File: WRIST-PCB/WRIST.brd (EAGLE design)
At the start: 56.3 x 16.5 mm, 44 parts, among them Q3 BSS138, U3 LP5907-2.8V

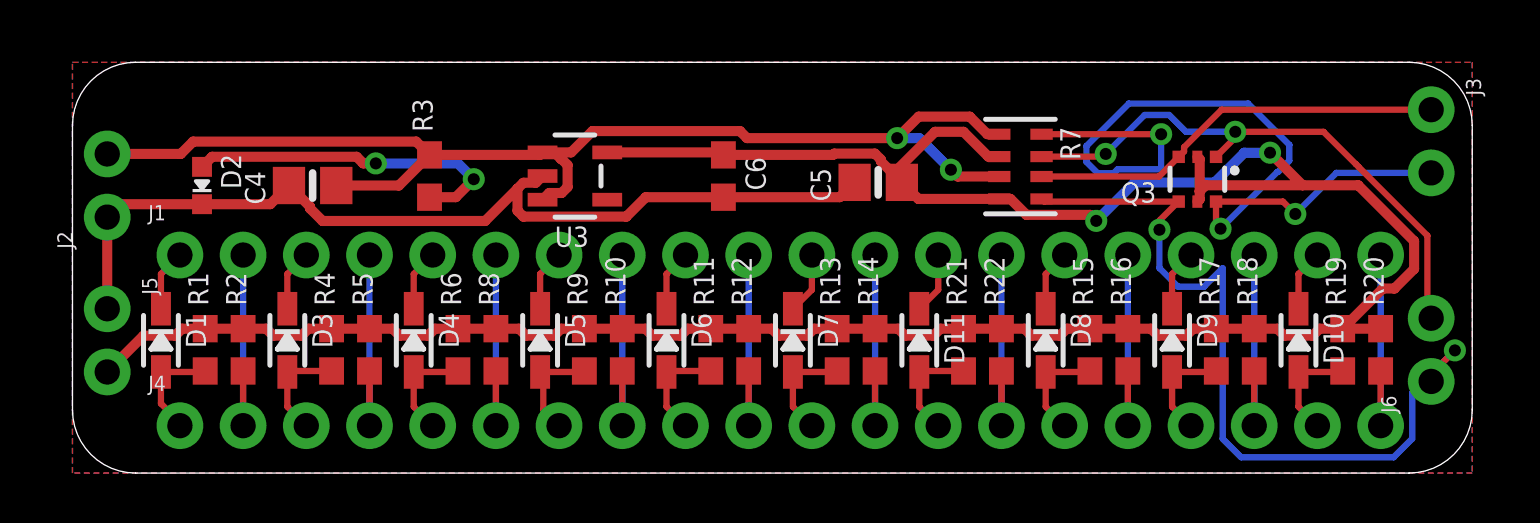
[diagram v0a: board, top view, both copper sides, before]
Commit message: update pcb through holes and design
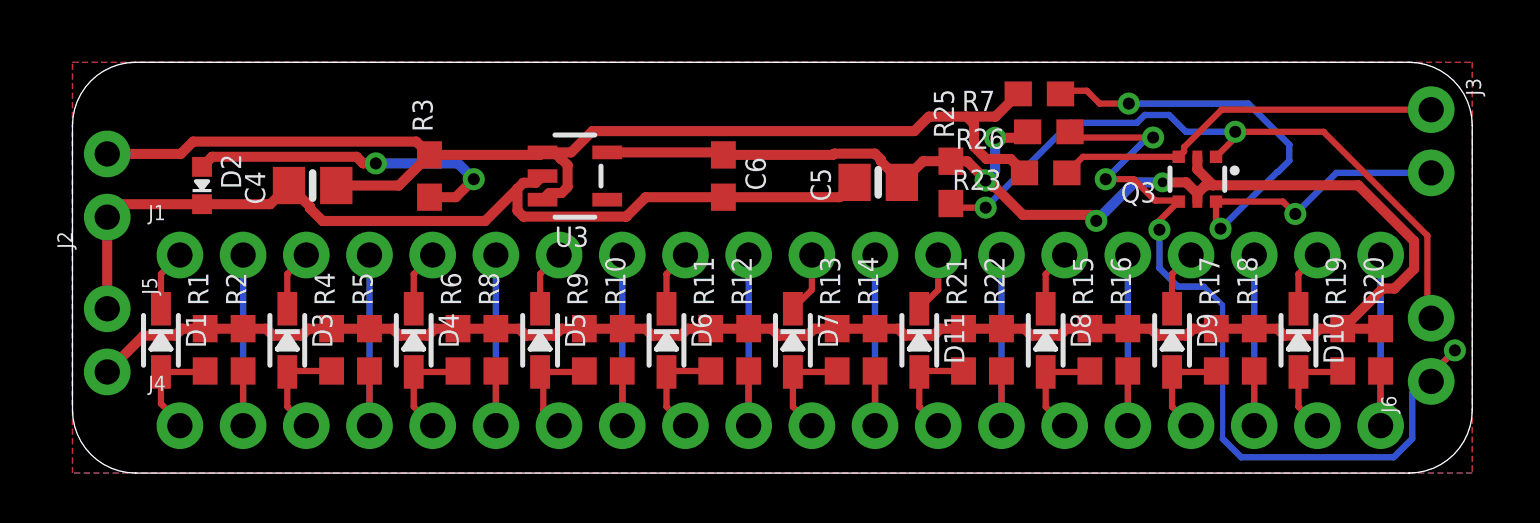
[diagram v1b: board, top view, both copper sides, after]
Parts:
- added R23, R25, R26: 10K, microbuilder:0603-NO
- R7: device microbuilder:RESPACK_4X0603 -> microbuilder:0603-NO
- moved R7 3.02 mm to (38.9, 15.2), turned to 180 degrees
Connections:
- net 2.8V: now also R25.2, R26.2; no longer R7.2, R7.4
- net SCL: now also R7.1; no longer R7.8
- net SCL_3V: now also R25.1; no longer R7.7
- net SDA: now also R23.1; no longer R7.6
- net SDA_3V: now also R26.1; no longer R7.5
- net VCC: now also R23.2, R7.2; no longer R7.1, R7.3
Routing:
- net SCL: track 34.9 -> 25.4 mm
- net 2.8V: track 106.7 -> 100.7 mm, vias 2 -> 4
- net SCL_3V: track 22.9 -> 27.5 mm
- net SDA_3V: track 32.7 -> 35.0 mm, vias 2 -> 4
- net SDA: track 16.9 -> 15.8 mm
- net VCC: track 49.8 -> 49.5 mm, vias 2 -> 0

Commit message: add text to wrist
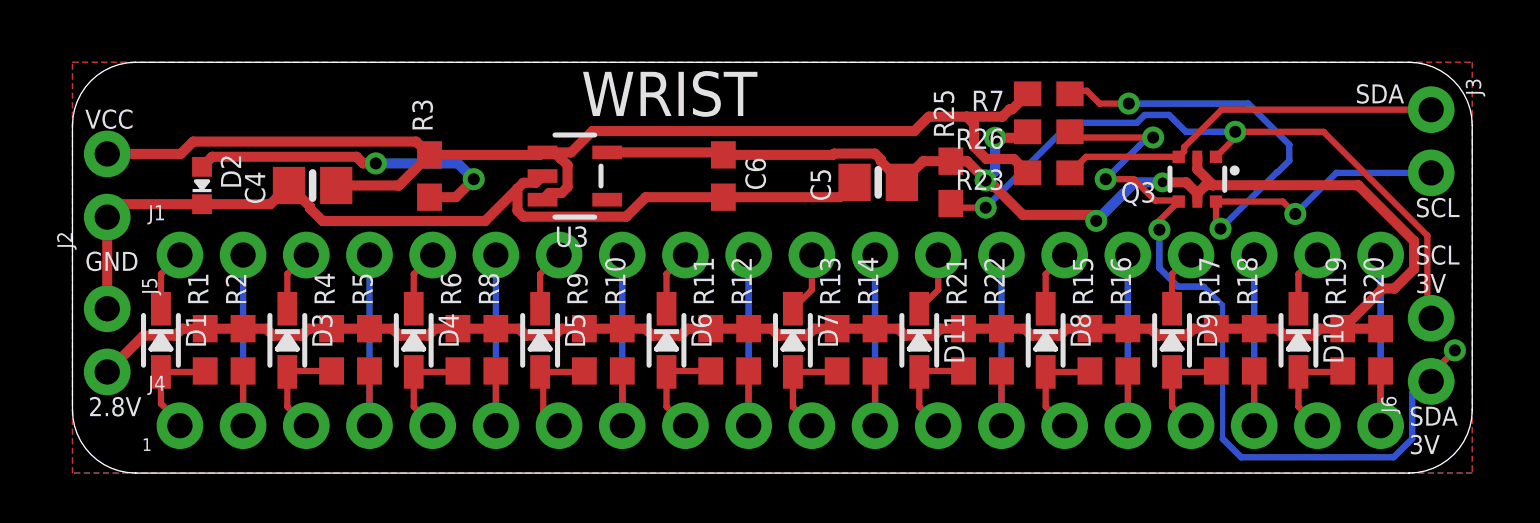
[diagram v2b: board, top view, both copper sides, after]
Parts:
- moved R7 0.38 mm to (39.2, 15.2)
- moved R23 0.13 mm to (39.2, 12.1)
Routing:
- net VCC: track 49.5 -> 50.0 mm
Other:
- board text added: "1"
- board text added: "2.8V"
- board text added: "GND"
- board text added: "SCL"
- board text added: "SCL 3V"
- board text added: "SDA"
- board text added: "SDA 3V"
- board text added: "VCC"
- board text added: "WRIST"
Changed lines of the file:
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@@
 <dimension x1="25.4" y1="9.144" x2="0" y2="6.223" x3="12.7" y3="-6.223" textsize="1.778" layer="47" dtype="horizontal" unit="inch"/>
 <dimension x1="13.208" y1="0" x2="12.319" y2="17.78" x3="32.131" y3="8.89" textsize="1.778" layer="47" dtype="vertical" unit="inch"/>
+<text x="0.508" y="13.843" size="0.762" layer="21">VCC</text>
+<text x="0.508" y="8.128" size="0.762" layer="21">GND</text>
+<text x="51.562" y="14.859" size="0.762" layer="21">SDA</text>
+<text x="53.975" y="10.287" size="0.762" layer="21">SCL</text>
+<text x="53.975" y="7.239" size="0.762" layer="21">SCL
+3V</text>
+<text x="53.721" y="0.762" size="0.762" layer="21">SDA
+3V</text>
+<text x="0.635" y="2.286" size="0.762" layer="21">2.8V</text>
+<text x="2.794" y="0.889" size="0.508" layer="21">1</text>
+<text x="20.447" y="14.351" size="1.778" layer="21">WRIST</text>
 </plain>
 <attributes>
@@
 <attribute name="VALUE" x="38.1" y="6.731" size="0.4064" layer="27" font="vector" ratio="10" rot="R90"/>
 </element>
-<element name="R7" library="microbuilder" package="0603-NO" value="10K" x="38.862" y="15.24" smashed="yes" rot="R180">
-<attribute name="NAME" x="37.084" y="15.367" size="0.8128" layer="25" font="vector" ratio="18" rot="R180"/>
-<attribute name="VALUE" x="37.084" y="16.002" size="0.4064" layer="27" font="vector" ratio="10" rot="R180"/>
-</element>
-<element name="R23" library="microbuilder" package="0603-NO" value="10K" x="39.116" y="12.065" smashed="yes" rot="R180">
-<attribute name="NAME" x="37.338" y="12.192" size="0.8128" layer="25" font="vector" ratio="18" rot="R180"/>
-<attribute name="VALUE" x="37.338" y="12.827" size="0.4064" layer="27" font="vector" ratio="10" rot="R180"/>
+<element name="R7" library="microbuilder" package="0603-NO" value="10K" x="39.243" y="15.24" smashed="yes" rot="R180">
+<attribute name="NAME" x="37.465" y="15.367" size="0.8128" layer="25" font="vector" ratio="18" rot="R180"/>
+<attribute name="VALUE" x="37.465" y="16.002" size="0.4064" layer="27" font="vector" ratio="10" rot="R180"/>
+</element>
+<element name="R23" library="microbuilder" package="0603-NO" value="10K" x="39.243" y="12.065" smashed="yes" rot="R180">
+<attribute name="NAME" x="37.465" y="12.192" size="0.8128" layer="25" font="vector" ratio="18" rot="R180"/>
+<attribute name="VALUE" x="37.465" y="12.827" size="0.4064" layer="27" font="vector" ratio="10" rot="R180"/>
 </element>
 <element name="R25" library="microbuilder" package="0603-NO" value="10K" x="35.306" y="11.684" smashed="yes" rot="R90">
@@
 <wire x1="46.189025" y1="14.605" x2="54.61" y2="14.605" width="0.254" layer="1"/>
 <contactref element="R23" pad="1"/>
-<wire x1="39.966" y1="12.065" x2="40.612" y2="12.711" width="0.254" layer="1"/>
-<wire x1="40.612" y1="12.711" x2="44.462" y2="12.711" width="0.254" layer="1"/>
+<wire x1="40.093" y1="12.065" x2="40.739" y2="12.711" width="0.254" layer="1"/>
+<wire x1="40.739" y1="12.711" x2="44.462" y2="12.711" width="0.254" layer="1"/>
 </signal>
 <signal name="SCL">
@@
 <wire x1="42.45730625" y1="14.8509" x2="41.2831" y2="14.8509" width="0.254" layer="1"/>
 <wire x1="41.2831" y1="14.8509" x2="40.767" y2="15.367" width="0.254" layer="1"/>
-<wire x1="40.767" y1="15.367" x2="39.839" y2="15.367" width="0.254" layer="1"/>
-<wire x1="39.839" y1="15.367" x2="39.712" y2="15.24" width="0.254" layer="1"/>
+<wire x1="40.767" y1="15.367" x2="40.22" y2="15.367" width="0.254" layer="1"/>
+<wire x1="40.22" y1="15.367" x2="40.093" y2="15.24" width="0.254" layer="1"/>
 </signal>
 <signal name="GND">
@@
 <contactref element="R23" pad="2"/>
 <wire x1="33.83729375" y1="13.7444" x2="34.41849375" y2="14.3256" width="0.4064" layer="1"/>
-<wire x1="37.0976" y1="14.3256" x2="38.012" y2="15.24" width="0.4064" layer="1"/>
 <wire x1="34.41849375" y1="14.3256" x2="35.941" y2="14.3256" width="0.4064" layer="1"/>
-<wire x1="35.941" y1="14.3256" x2="37.0976" y2="14.3256" width="0.4064" layer="1"/>
 <wire x1="20.8997625" y1="13.7444" x2="33.83729375" y2="13.7444" width="0.4064" layer="1"/>
 <wire x1="36.73154375" y1="12.6238" x2="36.2331" y2="13.12224375" width="0.4064" layer="1"/>
-<wire x1="38.266" y1="12.065" x2="37.7072" y2="12.6238" width="0.4064" layer="1"/>
-<wire x1="37.7072" y1="12.6238" x2="36.73154375" y2="12.6238" width="0.4064" layer="1"/>
+<wire x1="38.393" y1="12.065" x2="37.8342" y2="12.6238" width="0.4064" layer="1"/>
+<wire x1="37.8342" y1="12.6238" x2="36.73154375" y2="12.6238" width="0.4064" layer="1"/>
 <wire x1="36.2331" y1="13.12224375" x2="36.2331" y2="14.0335" width="0.4064" layer="1"/>
 <wire x1="36.2331" y1="14.0335" x2="35.941" y2="14.3256" width="0.4064" layer="1"/>
+<wire x1="38.393" y1="15.24" x2="37.7754" y2="14.6224" width="0.4064" layer="1"/>
+<wire x1="37.7754" y1="14.6224" x2="37.6746625" y2="14.6224" width="0.4064" layer="1"/>
+<wire x1="37.3778625" y1="14.3256" x2="35.941" y2="14.3256" width="0.4064" layer="1"/>
+<wire x1="37.6746625" y1="14.6224" x2="37.3778625" y2="14.3256" width="0.4064" layer="1"/>
 </signal>
 <signal name="N$1">
@@
 </drawing>
 <compatibility>
+<note version="6.3" minversion="6.2.2" severity="warning">
+Since Version 6.2.2 text objects can contain more than one line,
+which will not be processed correctly with this version.
+</note>
 <note version="8.2" severity="warning">
 Since Version 8.2, EAGLE supports online libraries. The ids

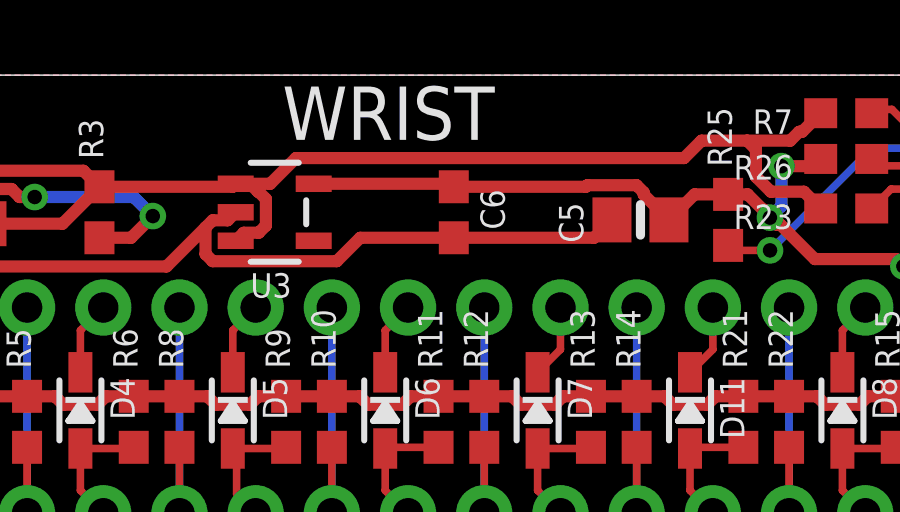
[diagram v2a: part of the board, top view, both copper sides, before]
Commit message: replace smt capacitor with holes
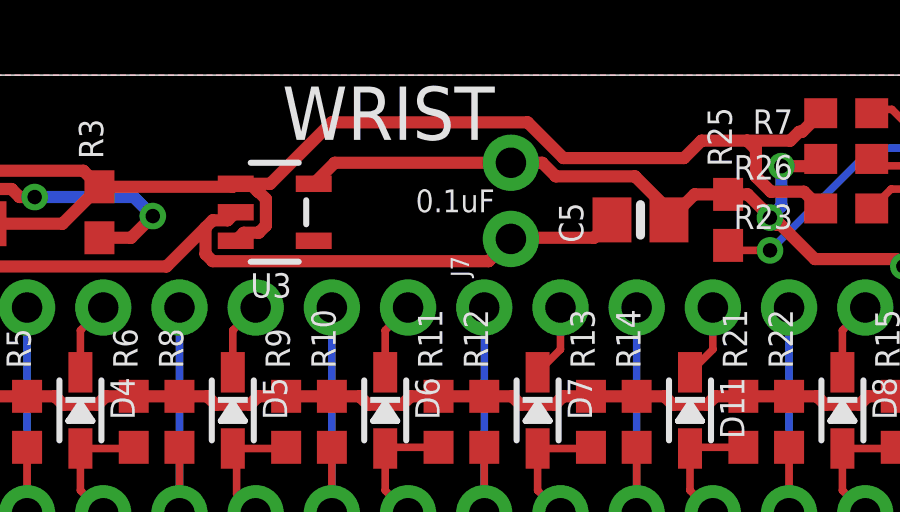
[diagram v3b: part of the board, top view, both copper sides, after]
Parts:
- removed C6: 0.1uF, microbuilder:0603-NO
- added J7: (no value), SparkFun-Connectors:1X02_NO_SILK
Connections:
- net 2.8V: now also J7.2; no longer C6.1
- net GND: now also J7.1; no longer C6.2
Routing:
- net VCC: track 50.0 -> 51.0 mm
- net 2.8V: track 100.7 -> 101.3 mm
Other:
- board text added: "0.1uF"
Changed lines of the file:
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@@
 <text x="2.794" y="0.889" size="0.508" layer="21">1</text>
 <text x="20.447" y="14.351" size="1.778" layer="21">WRIST</text>
+<text x="24.892" y="11.938" size="0.762" layer="21">0.1uF</text>
 </plain>
 <attributes>
@@
 <attribute name="VALUE" x="30.861" y="9.271" size="1.016" layer="27" ratio="10"/>
 </element>
-<element name="C6" library="microbuilder" package="0603-NO" value="0.1uF" x="26.162" y="11.938" smashed="yes" rot="R270">
-<attribute name="NAME" x="27.051" y="12.7" size="0.8128" layer="25" ratio="18" rot="R270"/>
-<attribute name="VALUE" x="26.67" y="13.335" size="1.016" layer="27" ratio="10" rot="R90"/>
-</element>
 <element name="Q3" library="microbuilder" package="SOT363" value="BSS138" x="45.212" y="11.811" smashed="yes" rot="R180">
 <attribute name="NAME" x="43.561" y="11.684" size="0.8128" layer="25" ratio="18" rot="R180"/>
@@
 <attribute name="NAME" x="37.465" y="13.843" size="0.8128" layer="25" font="vector" ratio="18" rot="R180"/>
 <attribute name="VALUE" x="37.465" y="14.478" size="0.4064" layer="27" font="vector" ratio="10" rot="R180"/>
+</element>
+<element name="J7" library="SparkFun-Connectors" library_urn="urn:adsk.eagle:library:513" package="1X02_NO_SILK" package3d_urn="urn:adsk.eagle:package:38051/1" value="" x="28.067" y="11.049" smashed="yes" rot="R90">
+<attribute name="NAME" x="26.67" y="9.779" size="0.6096" layer="25" font="vector" ratio="20" rot="R90"/>
+<attribute name="VALUE" x="30.099" y="9.779" size="0.6096" layer="27" font="vector" ratio="20" rot="R90"/>
 </element>
 </elements>
@@
 <contactref element="U3" pad="2"/>
 <contactref element="C5" pad="2"/>
-<contactref element="C6" pad="2"/>
 <polygon width="0.254" layer="1">
 <vertex x="0" y="16.51"/>
@@
 <wire x1="5.207" y1="10.807" x2="7.952" y2="10.807" width="0.4064" layer="1"/>
 <wire x1="7.952" y1="10.807" x2="8.702" y2="11.557" width="0.4064" layer="1"/>
-<wire x1="26.162" y1="11.088" x2="30.839" y2="11.088" width="0.4064" layer="1"/>
 <wire x1="30.839" y1="11.088" x2="31.435" y2="11.684" width="0.4064" layer="1"/>
-<wire x1="18.1245625" y1="10.3066" x2="17.8865" y2="10.5446625" width="0.4064" layer="1"/>
+<wire x1="17.8865" y1="10.5446625" x2="18.1245625" y2="10.3066" width="0.4064" layer="1"/>
 <wire x1="17.8865" y1="10.5446625" x2="17.8865" y2="11.4313375" width="0.4064" layer="1"/>
 <wire x1="17.8865" y1="11.4313375" x2="18.1245625" y2="11.6694" width="0.4064" layer="1"/>
-<wire x1="26.162" y1="11.088" x2="23.0428375" y2="11.088" width="0.4064" layer="1"/>
-<wire x1="23.0428375" y1="11.088" x2="22.2614375" y2="10.3066" width="0.4064" layer="1"/>
-<wire x1="22.2614375" y1="10.3066" x2="18.1245625" y2="10.3066" width="0.4064" layer="1"/>
 <wire x1="18.1245625" y1="11.6694" x2="18.6243" y2="11.6694" width="0.4064" layer="1"/>
 <wire x1="18.6243" y1="11.6694" x2="18.8929" y2="11.938" width="0.4064" layer="1"/>
@@
 <wire x1="10.0526625" y1="10.1316" x2="16.5867625" y2="10.1316" width="0.4064" layer="1"/>
 <wire x1="16.5867625" y1="10.1316" x2="17.8865" y2="11.4313375" width="0.4064" layer="1"/>
+<contactref element="J7" pad="1"/>
+<wire x1="27.3246" y1="10.3066" x2="28.067" y2="11.049" width="0.4064" layer="1"/>
+<wire x1="18.1245625" y1="10.3066" x2="27.3246" y2="10.3066" width="0.4064" layer="1"/>
+<wire x1="28.067" y1="11.049" x2="28.106" y2="11.088" width="0.4064" layer="1"/>
+<wire x1="28.106" y1="11.088" x2="30.839" y2="11.088" width="0.4064" layer="1"/>
 </signal>
 <signal name="XSHUT_1">
@@
 </signal>
 <signal name="2.8V">
-<contactref element="C6" pad="1"/>
 <contactref element="U3" pad="5"/>
 <contactref element="C5" pad="1"/>
@@
 <wire x1="2.8556" y1="5.5226" x2="4.1243375" y2="5.5226" width="0.4064" layer="1"/>
 <wire x1="4.1243375" y1="5.5226" x2="4.4047375" y2="5.803" width="0.4064" layer="1"/>
-<wire x1="21.4931" y1="12.888" x2="26.062" y2="12.888" width="0.4064" layer="1"/>
-<wire x1="26.062" y1="12.888" x2="26.162" y2="12.788" width="0.4064" layer="1"/>
-<wire x1="26.162" y1="12.788" x2="30.5642625" y2="12.788" width="0.4064" layer="1"/>
-<wire x1="30.5642625" y1="12.788" x2="30.6166625" y2="12.8404" width="0.4064" layer="1"/>
-<wire x1="30.6166625" y1="12.8404" x2="32.2533375" y2="12.8404" width="0.4064" layer="1"/>
-<wire x1="32.2533375" y1="12.8404" x2="32.4914" y2="12.6023375" width="0.4064" layer="1"/>
-<wire x1="32.4914" y1="12.6023375" x2="32.4914" y2="12.5276" width="0.4064" layer="1"/>
-<wire x1="32.4914" y1="12.5276" x2="33.335" y2="11.684" width="0.4064" layer="1"/>
 <wire x1="53.13561875" y1="7.4168" x2="53.9242" y2="8.20538125" width="0.4064" layer="1"/>
 <wire x1="53.9242" y1="8.20538125" x2="53.9242" y2="9.32061875" width="0.4064" layer="1"/>
@@
 <wire x1="44.7637375" y1="11.684" x2="45.212" y2="11.2357375" width="0.4064" layer="1"/>
 <wire x1="41.148" y1="10.1363" x2="42.6957" y2="11.684" width="0.4064" layer="16"/>
-<wire x1="33.335" y1="11.684" x2="34.185" y2="12.534" width="0.4064" layer="1"/>
+<wire x1="33.335" y1="11.684" x2="33.495" y2="11.844" width="0.4064" layer="1"/>
+<wire x1="33.495" y1="11.844" x2="34.185" y2="12.534" width="0.4064" layer="1"/>
 <wire x1="34.185" y1="12.534" x2="35.306" y2="12.534" width="0.4064" layer="1"/>
 <via x="36.69960625" y="11.7602" extent="1-16" drill="0.4826"/>
@@
 <wire x1="36.4790375" y1="12.0142" x2="36.56015625" y2="12.0142" width="0.4064" layer="1"/>
 <wire x1="36.56015625" y1="12.0142" x2="37.05545625" y2="11.5189" width="0.4064" layer="1"/>
+<contactref element="J7" pad="2"/>
+<wire x1="21.4931" y1="12.888" x2="22.1941" y2="13.589" width="0.4064" layer="1"/>
+<wire x1="22.1941" y1="13.589" x2="28.067" y2="13.589" width="0.4064" layer="1"/>
+<wire x1="28.067" y1="13.589" x2="29.1087125" y2="13.589" width="0.4064" layer="1"/>
+<wire x1="29.1087125" y1="13.589" x2="29.5629125" y2="13.1348" width="0.4064" layer="1"/>
+<wire x1="32.2042" y1="13.1348" x2="33.495" y2="11.844" width="0.4064" layer="1"/>
+<wire x1="29.5629125" y1="13.1348" x2="32.2042" y2="13.1348" width="0.4064" layer="1"/>
 </signal>
 <signal name="SCL_3V">
@@
 <wire x1="13.816" y1="13.323" x2="14.351" y2="12.788" width="0.4064" layer="1"/>
 <wire x1="18.8929" y1="12.888" x2="20.0433625" y2="12.888" width="0.4064" layer="1"/>
-<wire x1="20.0433625" y1="12.888" x2="20.8997625" y2="13.7444" width="0.4064" layer="1"/>
 <contactref element="R7" pad="2"/>
 <contactref element="R23" pad="2"/>
 <wire x1="33.83729375" y1="13.7444" x2="34.41849375" y2="14.3256" width="0.4064" layer="1"/>
 <wire x1="34.41849375" y1="14.3256" x2="35.941" y2="14.3256" width="0.4064" layer="1"/>
-<wire x1="20.8997625" y1="13.7444" x2="33.83729375" y2="13.7444" width="0.4064" layer="1"/>
 <wire x1="36.73154375" y1="12.6238" x2="36.2331" y2="13.12224375" width="0.4064" layer="1"/>
 <wire x1="38.393" y1="12.065" x2="37.8342" y2="12.6238" width="0.4064" layer="1"/>
@@
 <wire x1="37.3778625" y1="14.3256" x2="35.941" y2="14.3256" width="0.4064" layer="1"/>
 <wire x1="37.6746625" y1="14.6224" x2="37.3778625" y2="14.3256" width="0.4064" layer="1"/>
+<wire x1="29.81541875" y1="13.7444" x2="33.83729375" y2="13.7444" width="0.4064" layer="1"/>
+<wire x1="28.62461875" y1="14.9352" x2="29.81541875" y2="13.7444" width="0.4064" layer="1"/>
+<wire x1="22.0905625" y1="14.9352" x2="28.62461875" y2="14.9352" width="0.4064" layer="1"/>
+<wire x1="20.0433625" y1="12.888" x2="22.0905625" y2="14.9352" width="0.4064" layer="1"/>
 </signal>
 <signal name="N$1">
